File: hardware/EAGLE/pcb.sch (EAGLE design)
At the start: 45 parts, among them IC1 4017N, IC2 DG412DJD, IC3 DG412DJD, J1 2x5 pin header, Q1 MMBT3904, Q2 MMBT3904, Q3 MMBT3904, Q4 MMBT3904

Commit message: Transistor footprint fixed
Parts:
- removed Q1, Q2, Q3, Q4: MMBT3904, Transistor:NPN_MMBT3904-7-F_SOT-23
- added T1, T2, T3, T4: MMBT3904, transistor:MMBT3904LT1-NPN-SOT23-BEC
- C1, C2: value 100n -> 10u; device rcl:C-USC0603 -> rcl:CPOL-EU153CLV-0605
- C7, C8: value 10u -> 100n; device rcl:CPOL-EU153CLV-0605 -> rcl:C-USC0603
- D1, D2: value 1N4004 -> 1N4148WT; device Diodes:1N4004 -> diode:DIODE-SOD523
- D3, D4: value 1N4148WT -> 1N4004; device diode:DIODE-SOD523 -> Diodes:1N4004
- R12, R13, R16, R17, R19: value 10k -> 1k
- R14, R15, R18: value 47k -> 1k
- R2, R7, R8: value 1k -> 47k
- R3, R4, R5, R6, R9: value 1k -> 10k
- SV2: value 1x10 pin header -> 1x3 pin header; device con-lstb:MA10-1 -> con-lstb:MA03-1
- SV3: value 1x3 pin header -> 1x10 pin header; device con-lstb:MA03-1 -> con-lstb:MA10-1
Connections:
- net +12V: now also C1.+, C5.1, C7.1, D3.C, R3.2, R4.2, R5.2, R6.2, SV3.9; no longer C1.1, C2.1, C7.+, D1.C, R12.2, R13.2, R16.2, R17.2, SV2.9
- net -12V: now also C2.-, C6.2, C8.2, D4.A; no longer C3.2, C5.2, C8.-, D2.A
- net BUTTON: now also R9.1, SV3.6; no longer R19.1, SV2.6
- net CLK: now also D1.C, D6.C, R7.1; no longer D3.C, D7.C, R14.1
- net GND: now also C1.-, C2.+, C3.2, C5.2, C6.1, C7.2, C8.1, R7.2, R8.2, SV2.2, T1.E, T2.E, T3.E, T4.E; no longer C1.2, C2.2, C3.1, C5.1, C6.2, C7.-, C8.+, Q1.E, Q2.E, Q3.E, Q4.E, R14.2, R18.2, SV3.2
- net IO1A: now also R10.2; no longer R4.2
- net IO1B: now also R15.2, SV3.3; no longer R8.2, SV2.3
- net IO2A: now also R11.2; no longer R5.2
- net IO2B: now also R16.2, SV3.2; no longer R9.2, SV2.2
- net IO3A: now also R12.2; no longer R6.2
- net IO3B: now also R17.2, SV3.1; no longer R10.2, SV2.1
- net IO4A: now also R13.2, SV2.1; no longer R7.2, SV3.1
- net IO4B: now also R18.2, SV2.3; no longer R11.2, SV3.3
- net N$1: now also D3.A; no longer D1.A
- net N$10: now also R16.1; no longer R9.1
- net N$11: now also R17.1; no longer R10.1
- net N$12: now also R18.1; no longer R11.1
- net N$13: now also C3.1, D6.A, R9.2; no longer C6.1, D7.A, R19.2
- net N$14: now also T1.B; no longer Q1.B
- net N$15: now also R3.1, T1.C, T3.B; no longer Q1.C, Q2.B, R12.1
- net N$16: now also D1.A, R5.1, T3.C; no longer D3.A, Q2.C, R13.1
- net N$17: now also D7.A; no longer D4.A
- net N$19: now also R2.2, T2.B; no longer Q3.B, R15.2
- net N$2: now also D4.C; no longer D2.C
- net N$20: now also R4.1, T2.C, T4.B; no longer Q3.C, Q4.B, R16.1
- net N$21: now also D2.A, R6.1, T4.C; no longer D5.A, Q4.C, R17.1
- net N$3: now also R14.1; no longer R2.1
- net N$4: now also R10.1; no longer R4.1
- net N$5: now also R19.1; no longer R3.1
- net N$6: now also R11.1; no longer R5.1
- net N$7: now also R12.1; no longer R6.1
- net N$8: now also R13.1; no longer R7.1
- net N$9: now also R15.1; no longer R8.1
- net NO: now also D5.A; no longer D6.A
- net OIA: now also R14.2; no longer R2.2
- net OIB: now also R19.2, SV3.4; no longer R3.2, SV2.4
- net Q2: now also SV3.5, SV3.8; no longer SV2.5, SV2.8
- net Q3: now also SV3.7; no longer SV2.7
- net RES: now also D2.C, D7.C, R8.1; no longer D4.C, D6.C, R18.1
- net RESET: now also R2.1, SV3.10; no longer R15.1, SV2.10
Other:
- moved on the sheet: C3, C4, C5, C6, D5, D6, D7, R10, R11, R12, R13, R14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

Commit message: Fixed some layout issues
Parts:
- D1, D2, D5, D6, D7: value 1N4148WT -> 1N4148W; device diode:DIODE-SOD523 -> Diode:DIODE_1N4148W-7-F_SOD123G
- D3, D4: value 1N4004 -> (none); device Diodes:1N4004 -> diode:DIODE-SOD123
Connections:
- net N$17 renamed Q4
- net +12V: now also D4.C; no longer D3.C
- net -12V: now also D3.A; no longer D4.A
- net N$1: now also D4.A; no longer D3.A
- net N$2: now also D3.C; no longer D4.C

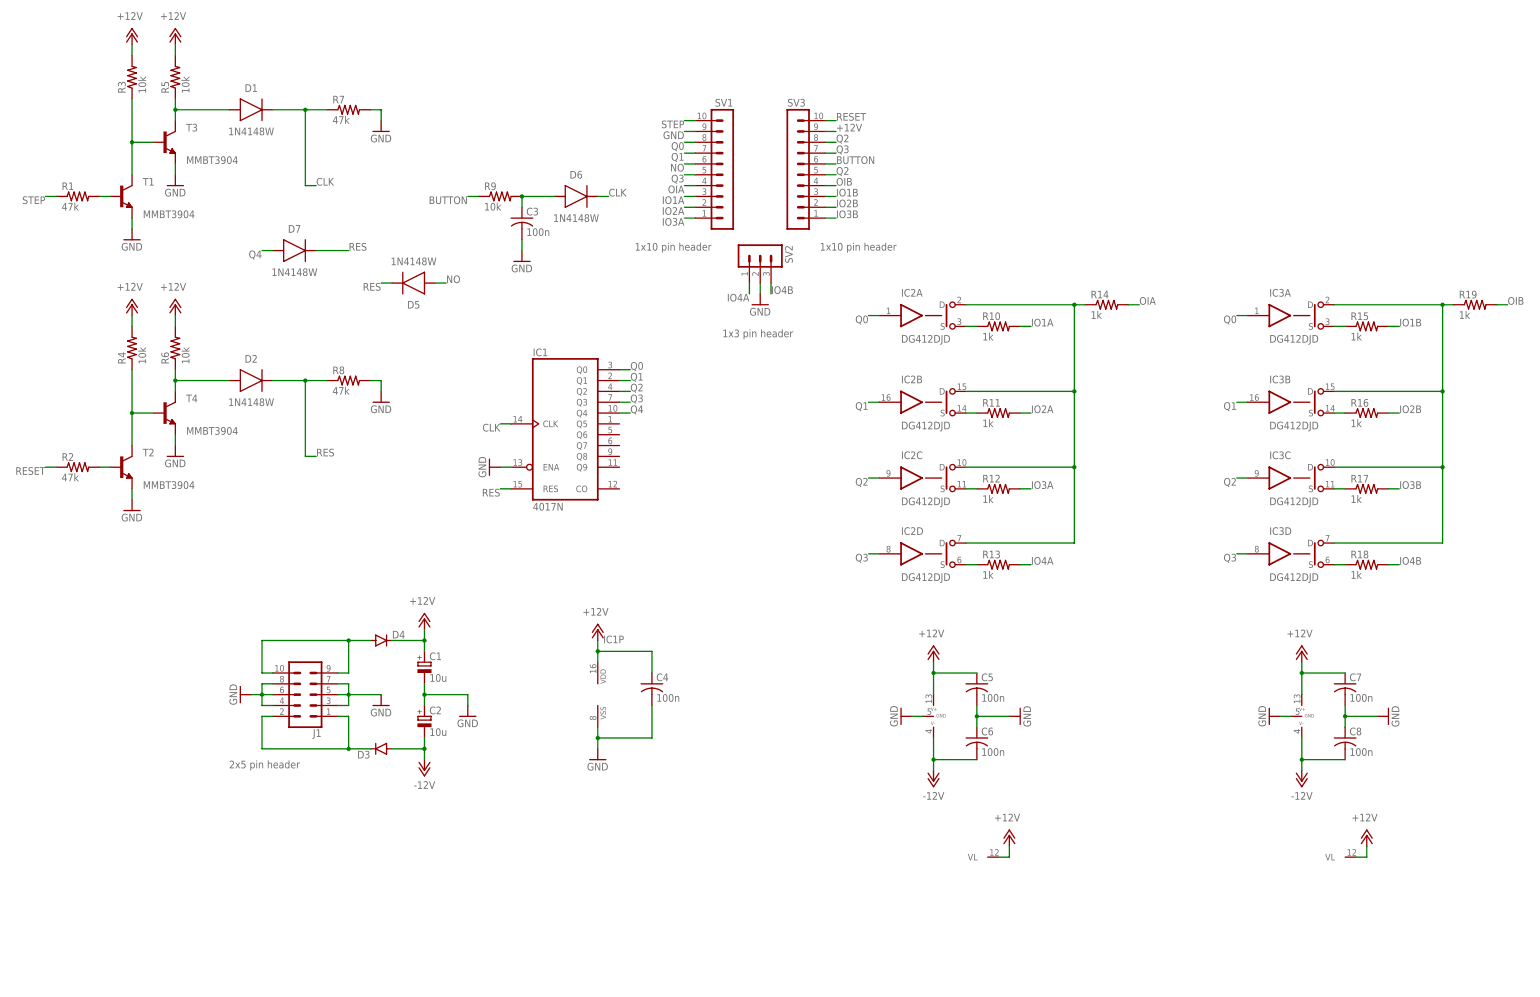
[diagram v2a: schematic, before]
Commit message: Added smd 4017 footprint
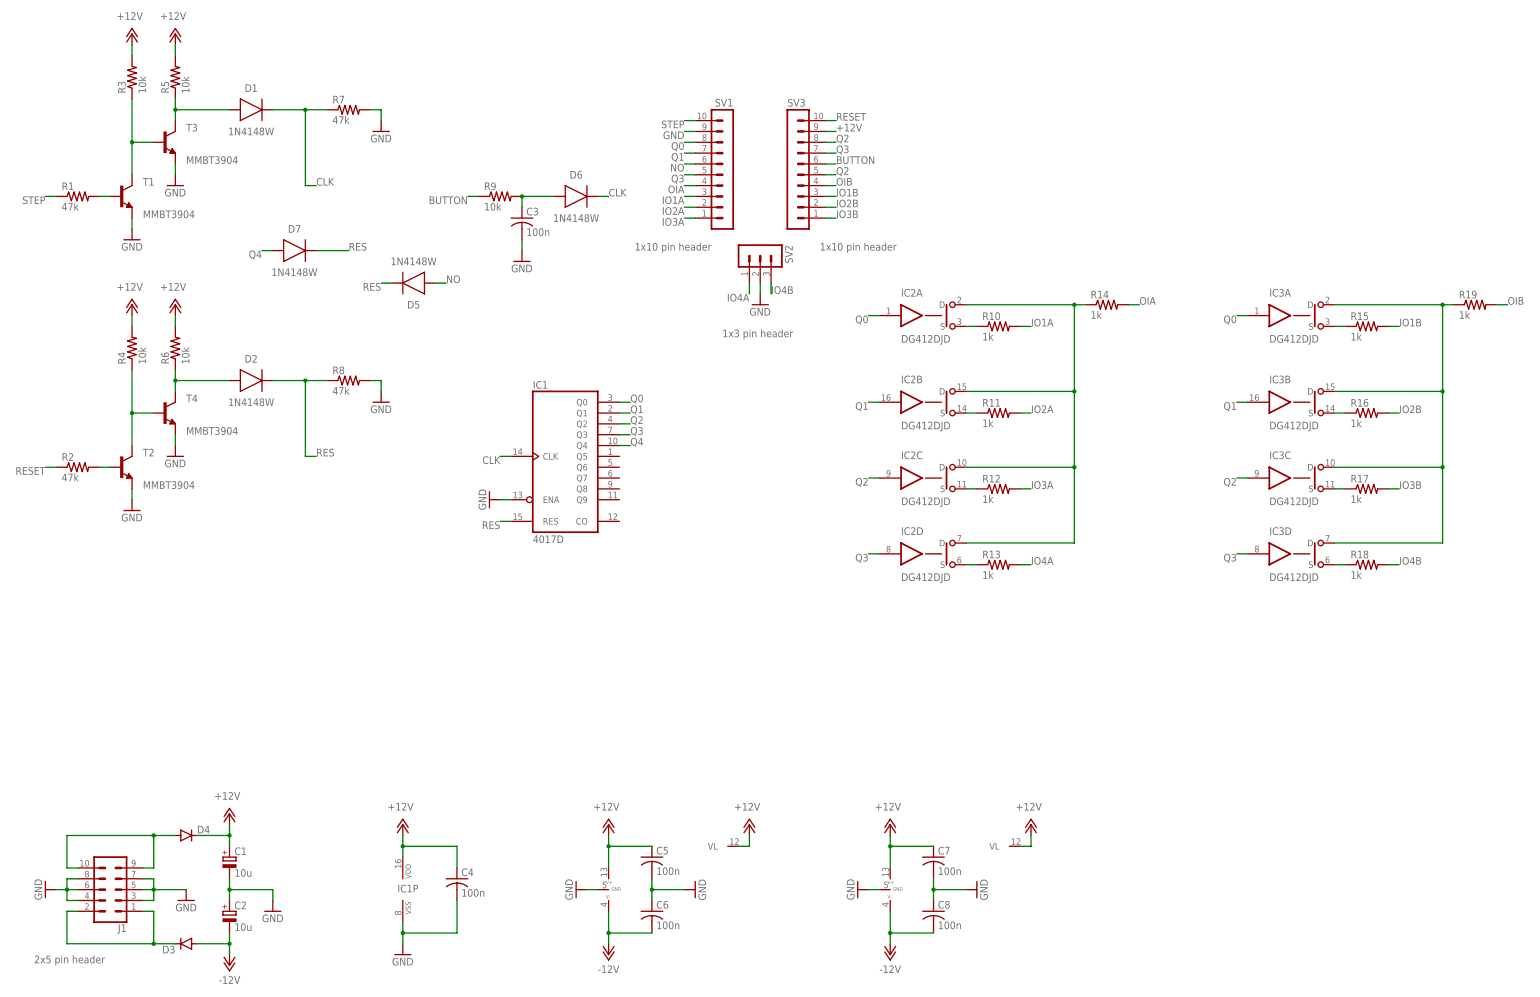
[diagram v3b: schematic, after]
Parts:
- IC1: value 4017N -> 4017D; device 40xx:4017N -> 40xx:4017D
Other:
- moved on the sheet: C1, C2, C4, C5, C6, C7, C8, D3, D4, IC1, IC1P, J1
